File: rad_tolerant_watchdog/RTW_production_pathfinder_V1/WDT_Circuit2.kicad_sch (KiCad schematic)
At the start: 27 parts, among them J12 Breakout, J13 Breakout, U3 TLV1704

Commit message: RTW V1 Pathfinder Layout Completed
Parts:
- added C15, C16, C19: 220u, Capacitor_Tantalum_SMD:CP_EIA-7361-38_AVX-V, symbol Device:C_Polarized_Small
- added D5: 1N4151WS, Diode_SMD:D_SOD-323, symbol oresat-diodes:1N4151WS-HE3
- added J16: Breakout, Connector_PinHeader_2.54mm:PinHeader_1x04_P2.54mm_Vertical, symbol Connector_Generic:Conn_01x04
- added R15: 10 (1206), Resistor_SMD:R_1206_3216Metric, symbol Device:R_Small_US
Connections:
- net GND: now also C15.2, C16.2, C19.2, J16.3 (Pin_3), J16.4 (Pin_4)
- net VBIAS_2: now also D5.2; no longer R50.1, R59.1, R65.2, U3.3 (V+)
- net WDT_WDI_2: now also J16.1 (Pin_1), J16.2 (Pin_2)
- new net: D5.1, R15.1
- new net WDT-VIN: C15.1, C16.1, C19.1, R15.2, R50.1, R59.1, R65.2, U3.3 (V+)
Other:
- note added: "Keeps WDT circuit powered through ~{ORESAT-SD} asserted period (~ 2-3 seconds)"

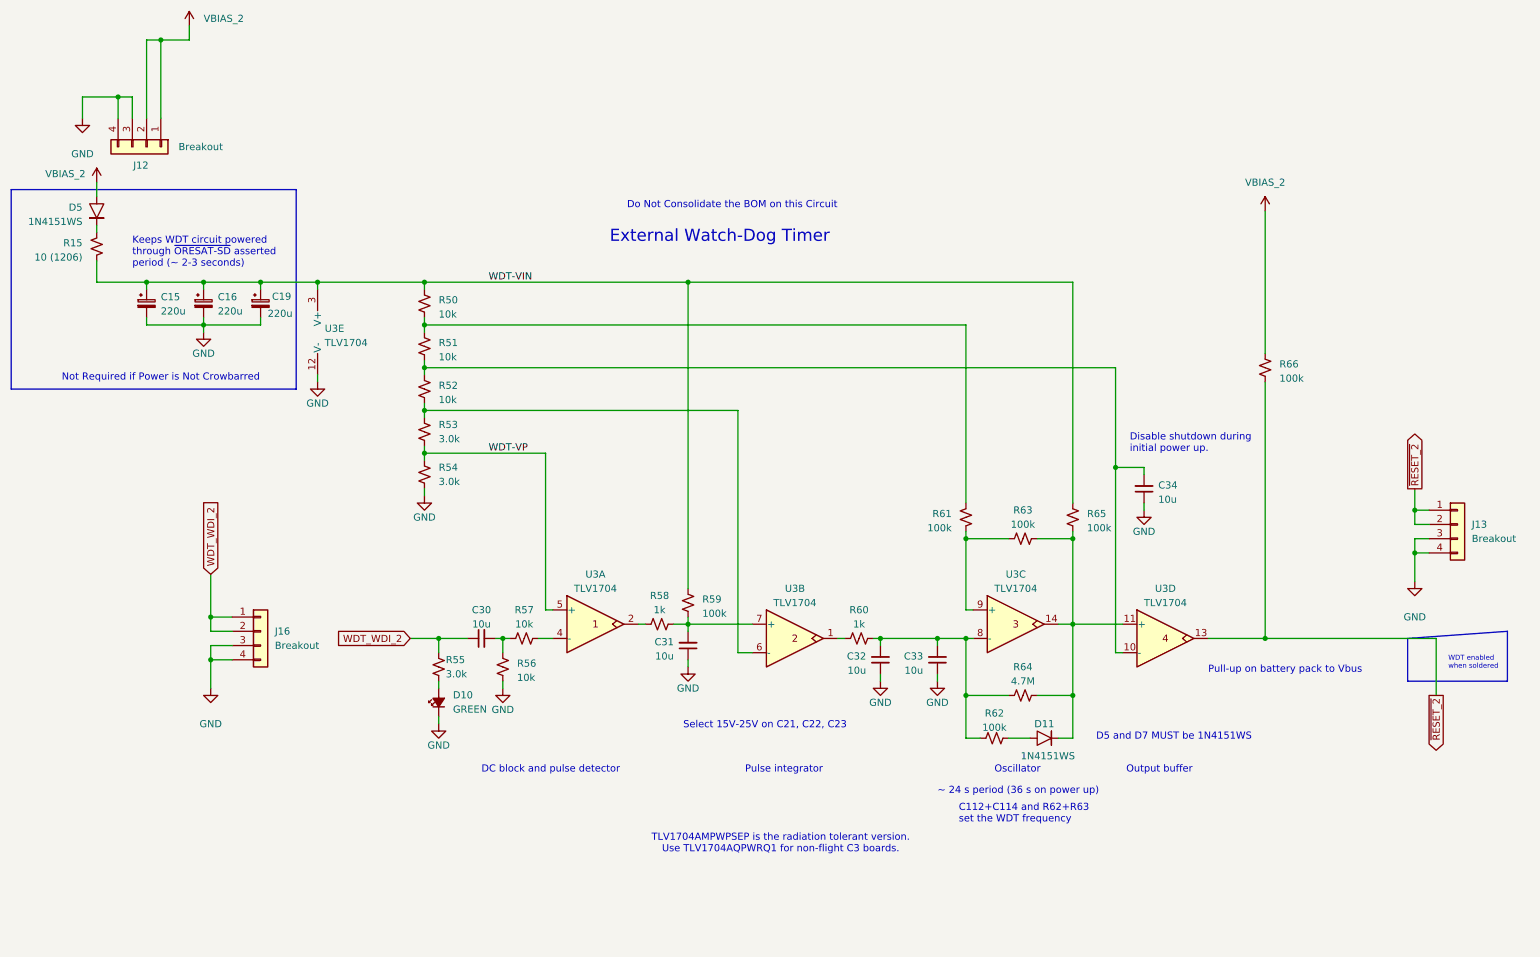
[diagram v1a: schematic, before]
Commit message: Added Decoupling Caps on VBIAS
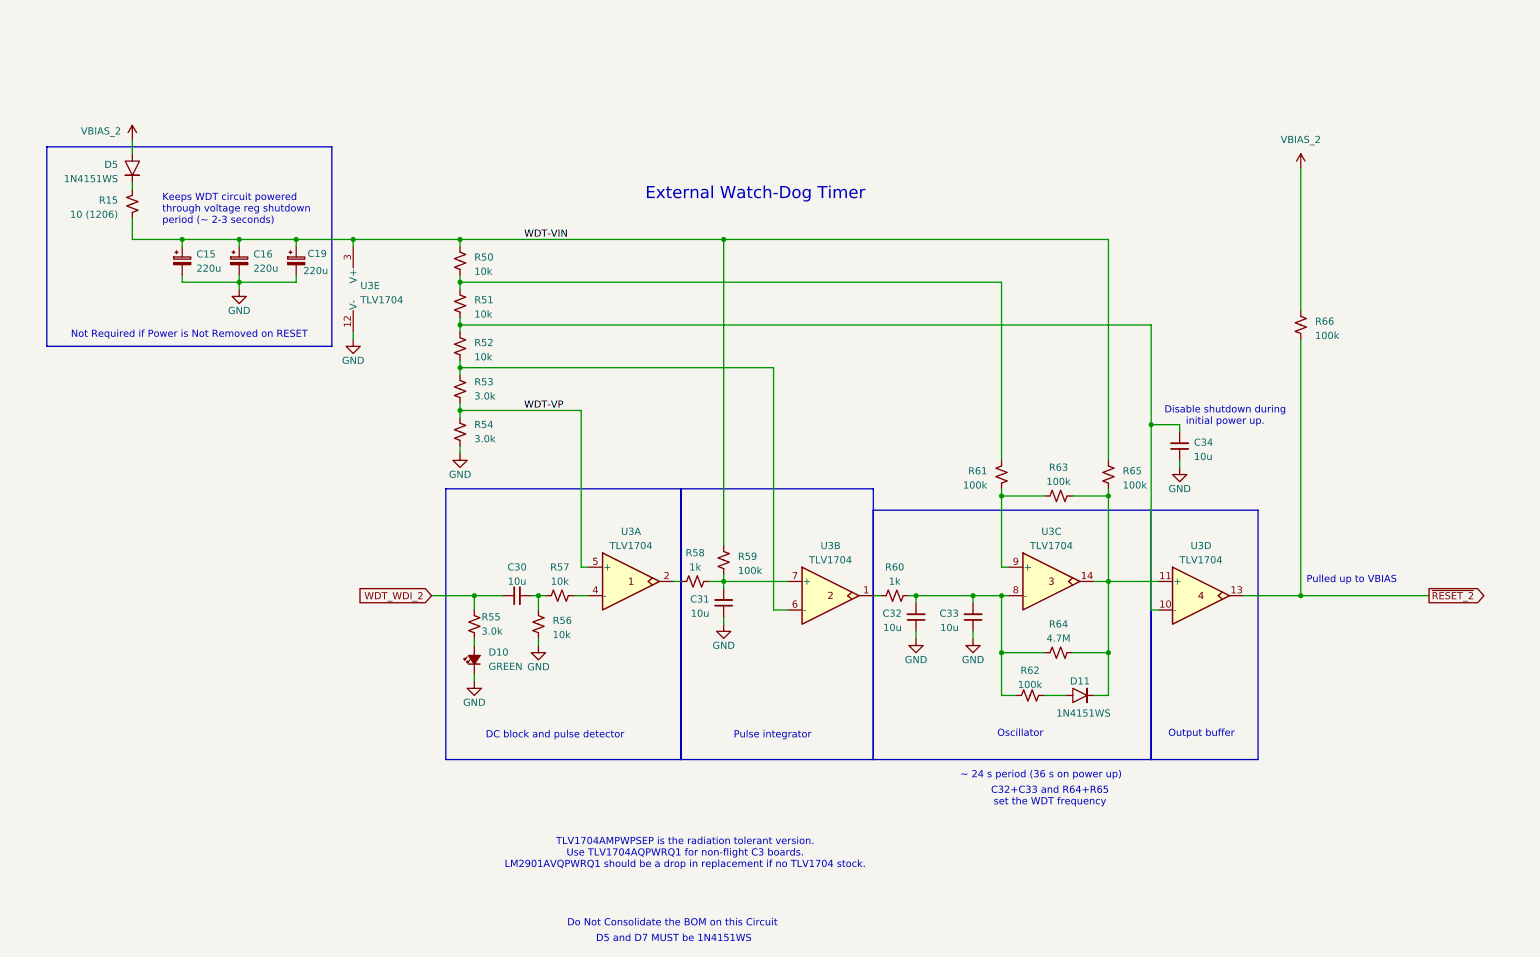
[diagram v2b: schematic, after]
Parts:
- removed J12, J13, J16: Breakout, Connector_PinHeader_2.54mm:PinHeader_1x04_P2.54mm_Vertical, symbol Connector_Generic:Conn_01x04
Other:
- note added: "C32+C33 and R64+R65 set the WDT frequency"
- note added: "Keeps WDT circuit powered through voltage reg shutdown period (~ 2-3 seconds)"
- note added: "Not Required if Power is Not Removed on RESET"
- note added: "Pulled up to VBIAS"
- note added: "TLV1704AMPWPSEP is the radiation tolerant version. Use TLV1704AQPWRQ1 for non-flight C3 boards. LM2901AVQPWRQ1 should be a drop in replacement if no TLV1704 stock."
- note removed: "C112+C114 and R62+R63 set the WDT frequency"
- note removed: "Keeps WDT circuit powered through ~{ORESAT-SD} asserted period (~ 2-3 seconds)"
- note removed: "Not Required if Power is Not Crowbarred"
- note removed: "Pull-up on battery pack to Vbus"
- note removed: "Select 15V-25V on C21, C22, C23"
- note removed: "TLV1704AMPWPSEP is the radiation tolerant version. Use TLV1704AQPWRQ1 for non-flight C3 boards."
- note removed: "WDT enabled when soldered"
- moved on the sheet: C15, C16, C19, C30, C31, C32, C33, C34, D10, D11, D5, R15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
